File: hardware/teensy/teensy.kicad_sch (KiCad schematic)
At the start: 99 parts, among them J4 CONN_083.5MM-8, J5 CONN_083.5MM-8, J6 CONN_083.5MM-8, J7 CONN_083.5MM-8, J8 CONN_023.5MM, J9 CONN_023.5MM, U1 Teensy3.5

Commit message: prettier traces, removed smt thing
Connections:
- net 3.3V: no longer D26.1 (K), D34.1 (K)
- net A9: now reaches D25.1 (K), D26.2 (A), R35.P$2 (2), U1.50 (23_A9_PWM_Touch)
- net A13: now reaches D3.1 (K), D4.2 (A), R24.P$2 (2), U1.24 (32_A13_TX4_SCK1)
- net A18: now reaches D10.2 (A), D9.1 (K), R27.P$2 (2), U1.34 (37_A18_PWM_SCL1)
- net A1: now reaches D19.1 (K), D20.2 (A), R32.P$2 (2), U1.42 (15_A1_CS0_Touch)
- net A6: now reaches D27.1 (K), D28.2 (A), R36.P$2 (2), U1.47 (20_A6_PWM_CS0_SCK1)
- net A4: now reaches D31.1 (K), D32.2 (A), R38.P$2 (2), U1.45 (18_A4_SDA0_Touch)
- net A22: now reaches D15.1 (K), D16.2 (A), R30.P$2 (2), U1.38 (A22_DAC1)
- net A5: now reaches D29.1 (K), D30.2 (A), R37.P$2 (2), U1.46 (19_A5_SCL0_Touch)
- net A2: now reaches D21.1 (K), D22.2 (A), R33.P$2 (2), U1.43 (16_A2_SCL0_Touch)
- net A16: now reaches D5.1 (K), D6.2 (A), R25.P$2 (2), U1.32 (35_A16_PWM)
- net A19: now reaches D11.1 (K), D12.2 (A), R28.P$2 (2), U1.35 (38_A19_PWM_SDA1)
- net A3: now reaches D23.1 (K), D24.2 (A), R34.P$2 (2), U1.44 (17_A3_SDA0_Touch)
- net A20: now reaches D13.1 (K), D14.2 (A), R29.P$2 (2), U1.36 (39_A20)
- net A12: now reaches D1.1 (K), D2.2 (A), R23.P$2 (2), U1.23 (31_A12_RX4_CS1)
- net A17: now reaches D7.1 (K), D8.2 (A), R26.P$2 (2), U1.33 (36_A17_PWM)
- net A0: now reaches D17.1 (K), D18.2 (A), R31.P$2 (2), U1.41 (14_A0_PWM_SCK0)
- net 3.3V_2: now reaches U1.51 (3.3V)
- net 3.3V_2: now also D26.1 (K), D34.1 (K)
- net L1_SCALED renamed A11_A7
- net L2_SCALED renamed A10_A8
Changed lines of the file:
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@@
   (junction (at 274.32 120.65) (diameter 0) (color 0 0 0 0))
   (junction (at 274.32 138.43) (diameter 0) (color 0 0 0 0))
-  (junction (at 274.32 156.21) (diameter 0) (color 0 0 0 0))
   (junction (at 276.86 234.95) (diameter 0) (color 0 0 0 0))
   (junction (at 279.4 120.65) (diameter 0) (color 0 0 0 0))
@@
   (junction (at 294.64 120.65) (diameter 0) (color 0 0 0 0))
   (junction (at 294.64 138.43) (diameter 0) (color 0 0 0 0))
-  (junction (at 294.64 156.21) (diameter 0) (color 0 0 0 0))
+  (junction (at 294.64 252.73) (diameter 0) (color 0 0 0 0))
   (junction (at 297.18 284.48) (diameter 0) (color 0 0 0 0))
   (junction (at 299.72 120.65) (diameter 0) (color 0 0 0 0))
@@
     (stroke (width 0) (type solid) (color 0 0 0 0))
   )
-  (wire (pts (xy 269.24 156.21) (xy 274.32 156.21))
+  (wire (pts (xy 269.24 156.21) (xy 279.4 156.21))
     (stroke (width 0) (type solid) (color 0 0 0 0))
   )
@@
     (stroke (width 0) (type solid) (color 0 0 0 0))
   )
-  (wire (pts (xy 274.32 151.13) (xy 274.32 156.21))
+  (wire (pts (xy 274.32 151.13) (xy 274.32 252.73))
     (stroke (width 0) (type solid) (color 0 0 0 0))
   )
-  (wire (pts (xy 274.32 156.21) (xy 279.4 156.21))
+  (wire (pts (xy 274.32 252.73) (xy 294.64 252.73))
     (stroke (width 0) (type solid) (color 0 0 0 0))
   )
@@
     (stroke (width 0) (type solid) (color 0 0 0 0))
   )
-  (wire (pts (xy 276.86 234.95) (xy 369.57 234.95))
+  (wire (pts (xy 276.86 234.95) (xy 368.3 234.95))
     (stroke (width 0) (type solid) (color 0 0 0 0))
   )
@@
     (stroke (width 0) (type solid) (color 0 0 0 0))
   )
-  (wire (pts (xy 289.56 156.21) (xy 294.64 156.21))
+  (wire (pts (xy 289.56 156.21) (xy 299.72 156.21))
     (stroke (width 0) (type solid) (color 0 0 0 0))
   )
@@
     (stroke (width 0) (type solid) (color 0 0 0 0))
   )
-  (wire (pts (xy 294.64 151.13) (xy 294.64 156.21))
+  (wire (pts (xy 294.64 252.73) (xy 294.64 151.13))
     (stroke (width 0) (type solid) (color 0 0 0 0))
   )
-  (wire (pts (xy 294.64 156.21) (xy 299.72 156.21))
+  (wire (pts (xy 294.64 252.73) (xy 388.62 252.73))
     (stroke (width 0) (type solid) (color 0 0 0 0))
   )
@@
     (stroke (width 0) (type solid) (color 0 0 0 0))
   )
-  (wire (pts (xy 365.76 217.17) (xy 369.57 217.17))
+  (wire (pts (xy 365.76 214.63) (xy 388.62 214.63))
+    (stroke (width 0) (type solid) (color 0 0 0 0))
+  )
+  (wire (pts (xy 365.76 217.17) (xy 368.3 217.17))
     (stroke (width 0) (type solid) (color 0 0 0 0))
   )
@@
     (stroke (width 0) (type solid) (color 0 0 0 0))
   )
-  (wire (pts (xy 369.57 217.17) (xy 369.57 234.95))
+  (wire (pts (xy 368.3 217.17) (xy 368.3 234.95))
     (stroke (width 0) (type solid) (color 0 0 0 0))
   )
@@
     (stroke (width 0) (type solid) (color 0 0 0 0))
   )
+  (wire (pts (xy 388.62 214.63) (xy 388.62 252.73))
+    (stroke (width 0) (type solid) (color 0 0 0 0))
+  )
   (label "L2" (at 83.82 284.48 180)
     (effects (font (size 1.27 1.27)) (justify right bottom))
@@
     (effects (font (size 1.27 1.27)) (justify right bottom))
   )
+  (label "A12" (at 306.07 176.53 180)
+    (effects (font (size 1.27 1.27)) (justify right bottom))
+  )
+  (label "A13" (at 306.07 179.07 180)
+    (effects (font (size 1.27 1.27)) (justify right bottom))
+  )
+  (label "A16" (at 306.07 199.39 180)
+    (effects (font (size 1.27 1.27)) (justify right bottom))
+  )
+  (label "A17" (at 306.07 201.93 180)
+    (effects (font (size 1.27 1.27)) (justify right bottom))
+  )
+  (label "A18" (at 306.07 204.47 180)
+    (effects (font (size 1.27 1.27)) (justify right bottom))
+  )
+  (label "A19" (at 306.07 207.01 180)
+    (effects (font (size 1.27 1.27)) (justify right bottom))
+  )
+  (label "A20" (at 306.07 209.55 180)
+    (effects (font (size 1.27 1.27)) (justify right bottom))
+  )
+  (label "A22" (at 306.07 214.63 180)
+    (effects (font (size 1.27 1.27)) (justify right bottom))
+  )
+  (label "A0" (at 306.07 222.25 180)
+    (effects (font (size 1.27 1.27)) (justify right bottom))
+  )
+  (label "A1" (at 306.07 224.79 180)
+    (effects (font (size 1.27 1.27)) (justify right bottom))
+  )
+  (label "A2" (at 306.07 227.33 180)
+    (effects (font (size 1.27 1.27)) (justify right bottom))
+  )
+  (label "A3" (at 306.07 229.87 180)
+    (effects (font (size 1.27 1.27)) (justify right bottom))
+  )
+  (label "A9" (at 368.3 217.17 180)
+    (effects (font (size 1.27 1.27)) (justify right bottom))
+  )
+  (label "3.3V_2" (at 372.11 214.63 180)
+    (effects (font (size 1.27 1.27)) (justify right bottom))
+  )
+  (label "A4" (at 372.11 229.87 180)
+    (effects (font (size 1.27 1.27)) (justify right bottom))
+  )
+  (label "A11_A7" (at 373.38 199.39 180)
+    (effects (font (size 1.27 1.27)) (justify right bottom))
+  )
+  (label "A10_A8" (at 373.38 201.93 180)
+    (effects (font (size 1.27 1.27)) (justify right bottom))
+  )
+  (label "A6" (at 373.38 224.79 180)
+    (effects (font (size 1.27 1.27)) (justify right bottom))
+  )
+  (label "A5" (at 373.38 227.33 180)
+    (effects (font (size 1.27 1.27)) (justify right bottom))
+  )
   (symbol (lib_id "SparkFun-Resistors:RESISTORAXIAL-0.3") (at 118.11 176.53 0) (unit 1)
     (in_bom yes) (on_board yes)
@@
       (effects (font (size 1.27 1.27)) hide)
     )
-    (property "Footprint" "teensy:Teensy35_36" (id 2) (at 336.55 175.26 0)
+    (property "Footprint" "teensy:Teensy35_36_EMON" (id 2) (at 336.55 175.26 0)
       (effects (font (size 1.27 1.27)) hide)
     )

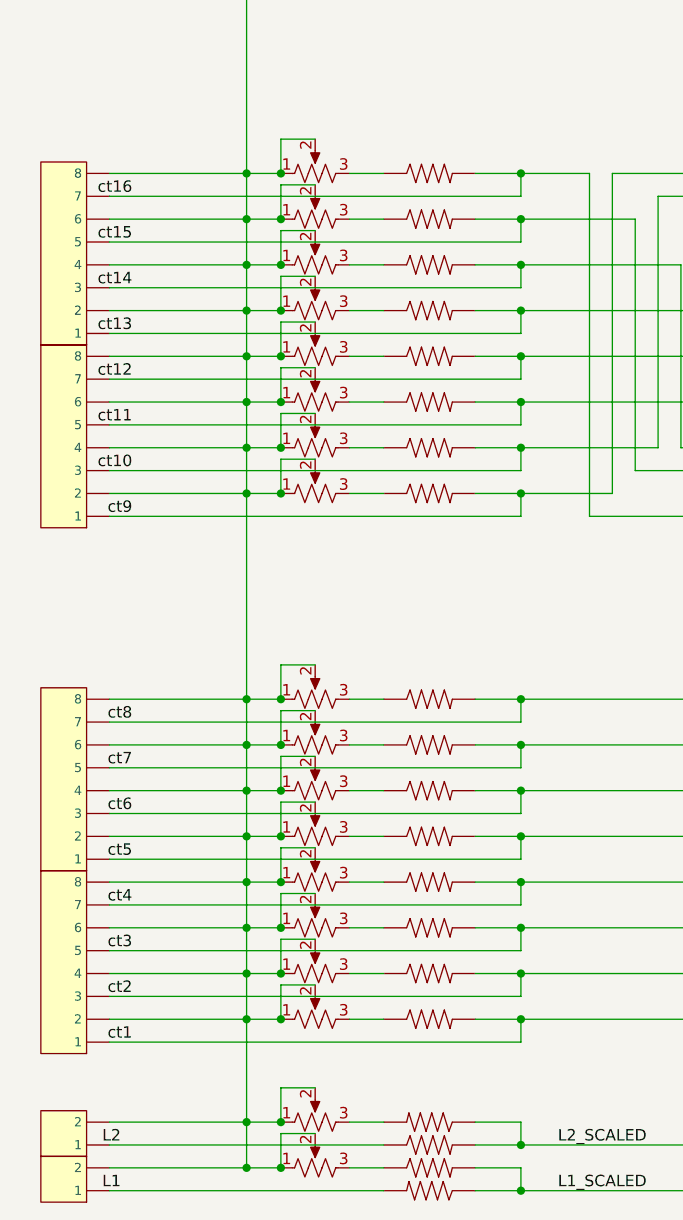
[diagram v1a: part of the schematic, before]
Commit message: 2.54 rather than 3.5mm screws, now fits in 3x5
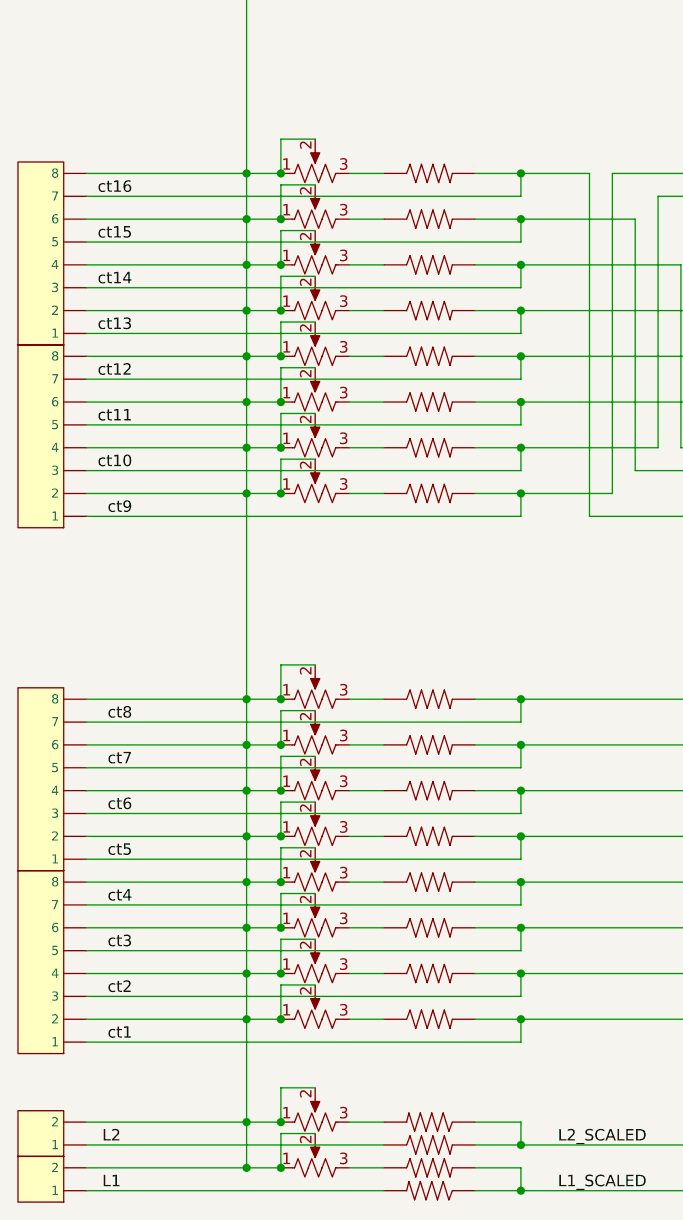
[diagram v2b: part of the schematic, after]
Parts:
- removed J4, J5, J6, J7: CONN_083.5MM-8, Connectors:SCREWTERMINAL-3.5MM-8, symbol SparkFun-Connectors:CONN_083.5MM-8
- removed J8, J9: CONN_023.5MM, Connectors:SCREWTERMINAL-3.5MM-2, symbol SparkFun-Connectors:CONN_023.5MM
- added J1, J2, J3, J4: CONN_08NO_SILK_FEMALE_PTH, Connectors:1X08_NO_SILK, symbol SparkFun-Connectors:CONN_08NO_SILK_FEMALE_PTH
- added J5, J6: CONN_02, Connectors:1X02_NO_SILK, symbol SparkFun-Connectors:CONN_02
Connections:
- net CT_BIAS: now also J1.2, J1.4, J1.6, J1.8, J2.2, J2.4, J2.6, J2.8, J3.2, J3.4, J3.6, J3.8, J4.2, J4.4, J4.6, J4.8, J5.2, J6.2
- net L1: now also J6.1
- net L2: now also J5.1
- net ct1: now also J4.1
- net ct10: now also J2.3
- net ct11: now also J2.5
- net ct12: now also J2.7
- net ct13: now also J1.1
- net ct14: now also J1.3
- net ct15: now also J1.5
- net ct16: now also J1.7
- net ct2: now also J4.3
- net ct3: now also J4.5
- net ct4: now also J4.7
- net ct5: now also J3.1
- net ct6: now also J3.3
- net ct7: now also J3.5
- net ct8: now also J3.7
- net ct9: now also J2.1

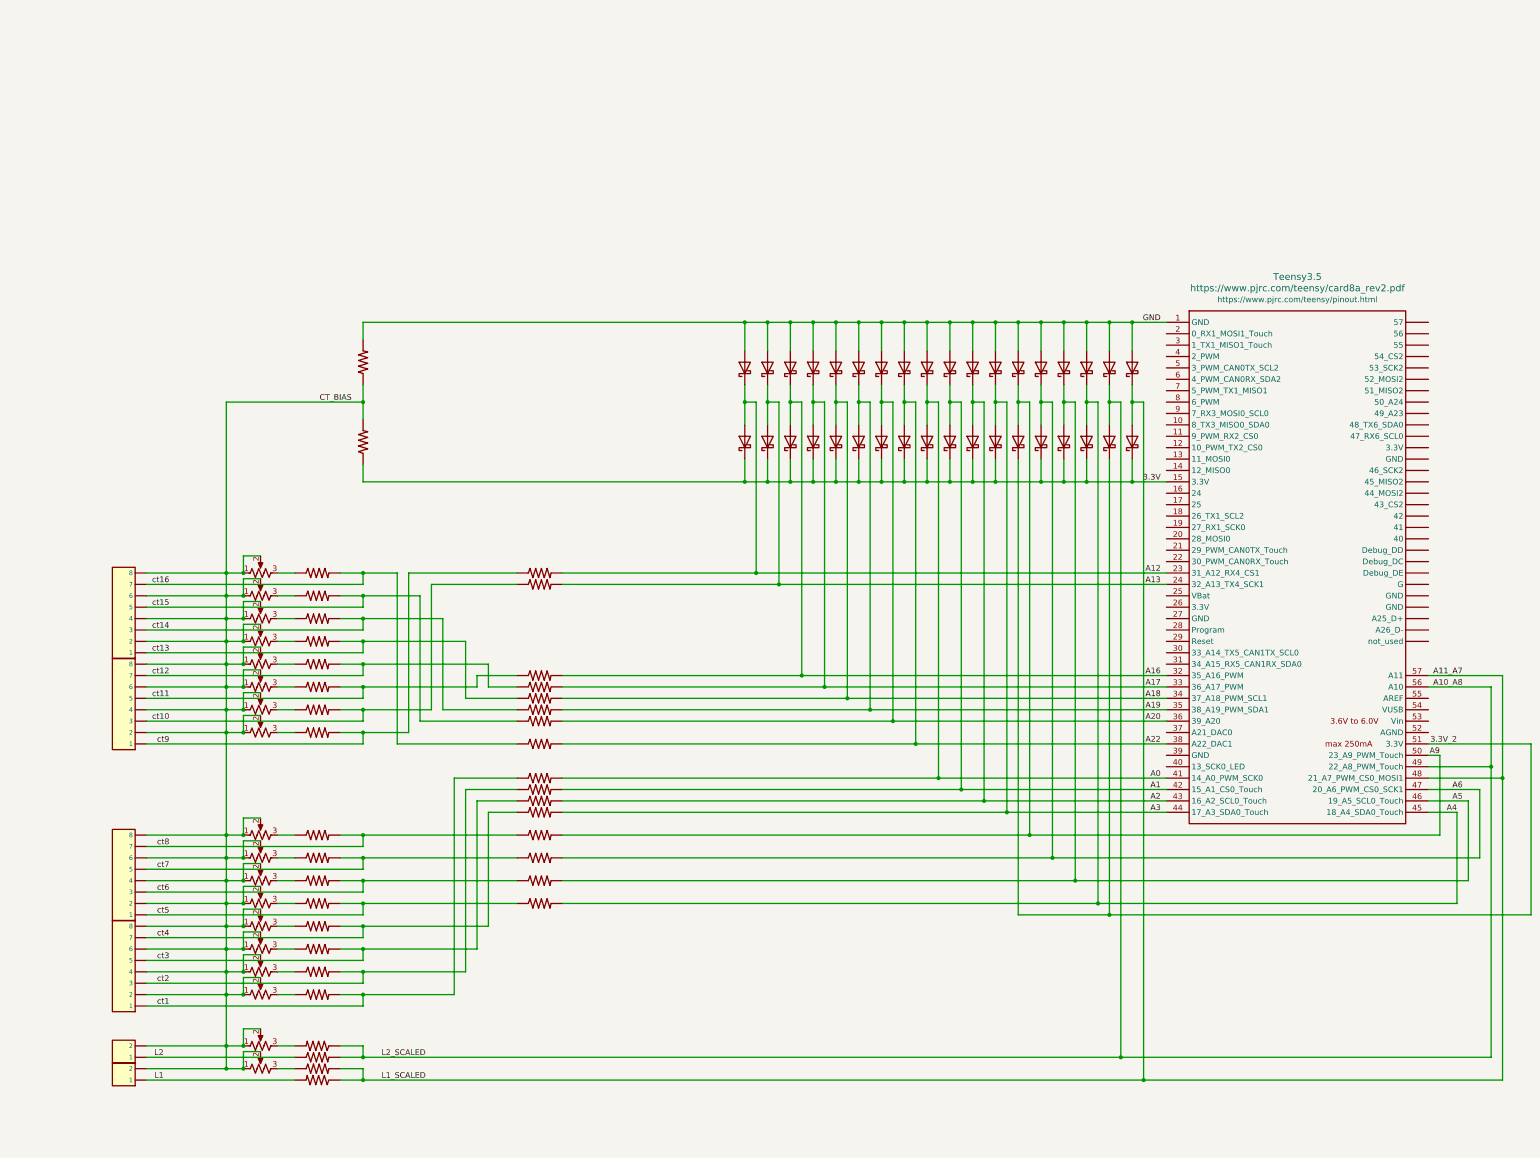
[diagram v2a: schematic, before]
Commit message: removed some resistors i don't need
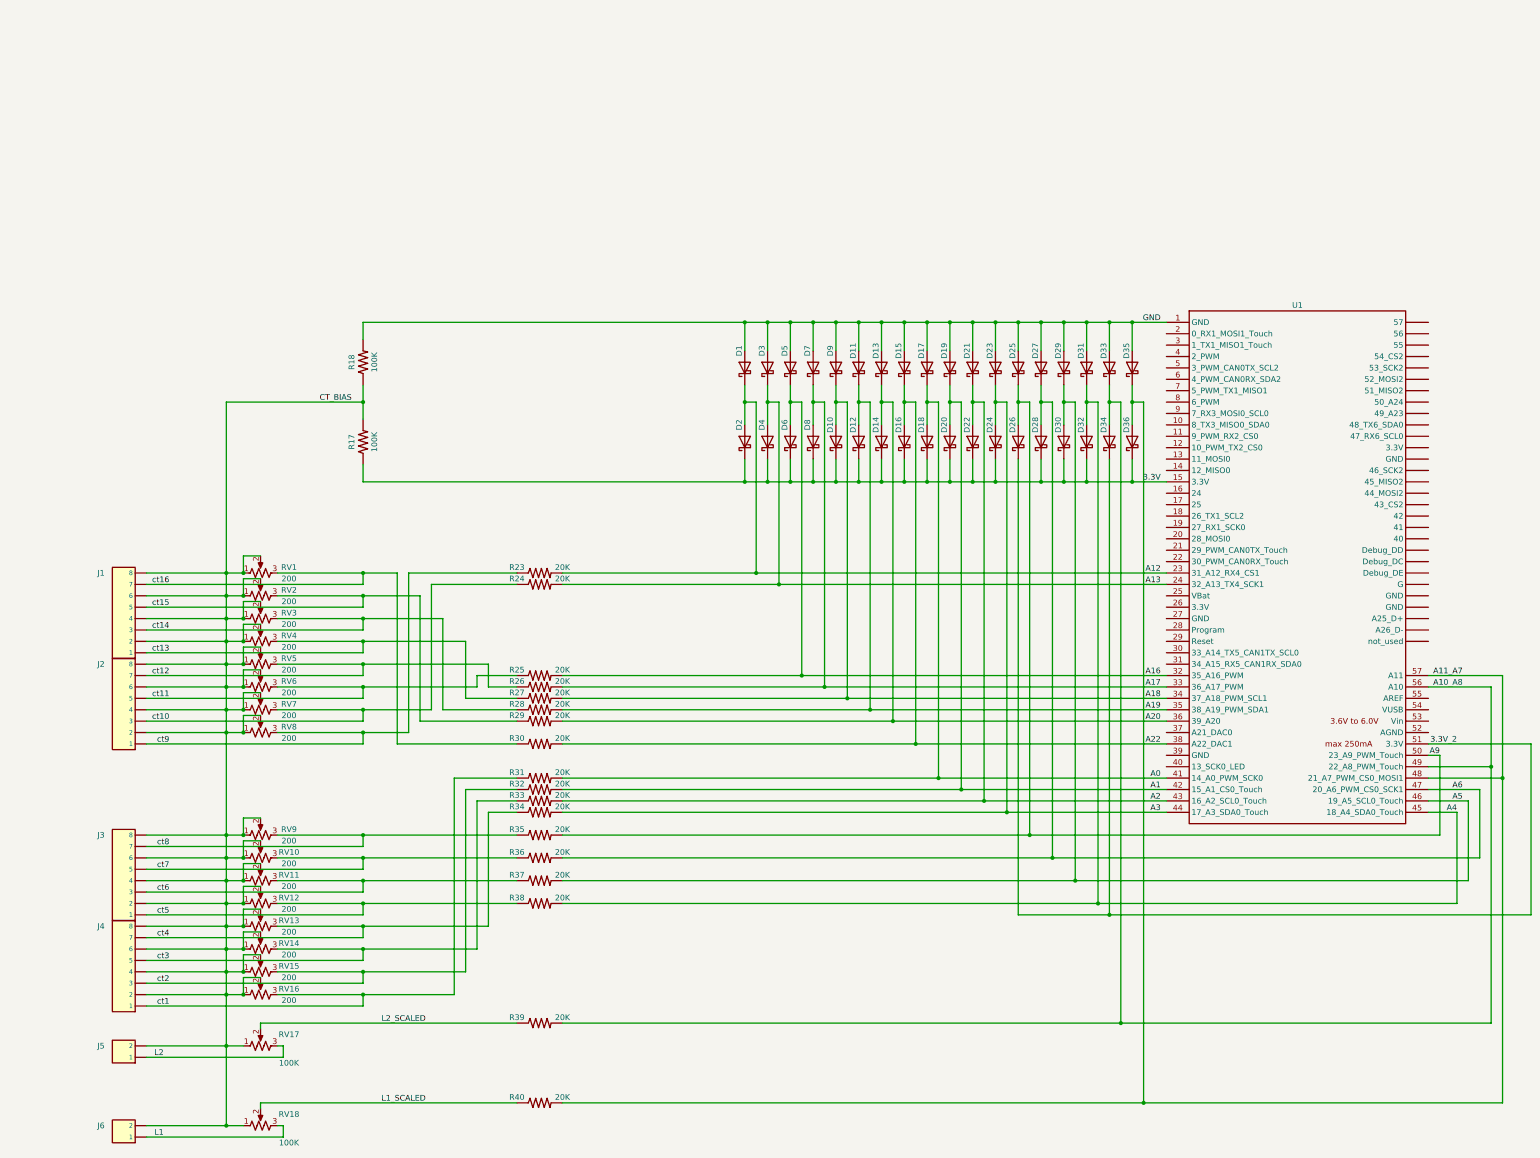
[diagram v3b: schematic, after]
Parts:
- removed R1, R10, R11, R12, R13, R14, R15, R16, R19, R2, R20, R21, R22, R3, R4, R5, R6, R7, R8, R9: RESISTORAXIAL-0.3, Resistors:AXIAL-0.3, symbol SparkFun-Resistors:RESISTORAXIAL-0.3
- added R39, R40: 20K, Resistors:AXIAL-0.3, symbol SparkFun-Resistors:RESISTORAXIAL-0.3
- D1, D10, D11, D12, D13, D14, D15, D16, D17, D18, D19, D2, D20, D21, D22, D23, D24, D25, D26, D27, D28, D29, D3, D30, D31, D32, D33, D34, D35, D36, D4, D5, D6, D7, D8, D9: value D_Schottky -> ~
- J1, J2, J3, J4: value CONN_08NO_SILK_FEMALE_PTH -> ~; footprint Connectors:1X08_NO_SILK -> Connectors:1X08; Field4 CONN-08438 -> (none)
- J5, J6: value CONN_02 -> ~; footprint Connectors:1X02_NO_SILK -> Connectors:1X02; Field4 XXX-00000 -> (none)
- R17, R18: value RESISTORAXIAL-0.3 -> 100K; Field4 (none) -> (none)
- R23, R24, R25, R26, R27, R28, R29, R30, R31, R32, R33, R34, R35, R36, R37, R38: value RESISTORAXIAL-0.3 -> 20K; Field4 (none) -> (none)
- RV1, RV10, RV11, RV12, RV13, RV14, RV15, RV16, RV2, RV3, RV4, RV5, RV6, RV7, RV8, RV9: value R_POT_US -> 200
- RV17, RV18: value R_POT_US -> 100K
- U1: footprint teensy:Teensy35_36 -> teensy:Teensy35_36_EMON
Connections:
- net A10_A8: now also R39.P$2 (2)
- net A11_A7: now also R40.P$2 (2)
- net CT_BIAS: no longer RV17.2, RV18.2
- net L1: now also RV18.3
- net L2: now also RV17.3
- net ct1: now also RV16.3
- net ct10: now also RV7.3
- net ct11: now also RV6.3
- net ct12: now also RV5.3
- net ct13: now also RV4.3
- net ct14: now also RV3.3
- net ct15: now also RV2.3
- net ct16: now also RV1.3
- net ct2: now also RV15.3
- net ct3: now also RV14.3
- net ct4: now also RV13.3
- net ct5: now also RV12.3
- net ct6: now also RV11.3
- net ct7: now also RV10.3
- net ct8: now also RV9.3
- net ct9: now also RV8.3
- new net L1_SCALED: R40.P$1 (1), RV18.2
- new net L2_SCALED: R39.P$1 (1), RV17.2

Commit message: formatting for printing
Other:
- moved on the sheet: D1, D10, D11, D12, D13, D14, D15, D16, D17, D18, D19, D2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

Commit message: add capacitor for bias smoothing
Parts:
- added C1, C2: 100uF, Resistors:AXIAL-0.3, symbol SparkFun-Capacitors:100UF-POLAR-10X10.5-63V-20%
